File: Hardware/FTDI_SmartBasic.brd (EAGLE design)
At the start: 35.6 x 20.3 mm, 28 parts, among them U1 FT232RLSSOP, U2 MIC5219 3.3V, U3 TS3USB221A

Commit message: Incorporate changes from review
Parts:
- LOGO2: value SFE_LOGO_NAME_FLAME.1_INCH -> SFE_LOGO_FLAME.2_INCH; device SparkFun-Aesthetics:SFE_LOGO_NAME_FLAME_.1 -> SparkFun-Aesthetics:SFE_LOGO_FLAME_.2
- moved LOGO2 5.22 mm to (7.24, 6.60)
- moved JP3 1.27 mm to (14.0, 1.27)
- moved JP2 0.25 mm to (30.5, 1.27)
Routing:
- net V_OUT: track 82.6 -> 81.3 mm
- net N$17: track 15.6 -> 16.9 mm
- net N$16: track 18.5 -> 19.7 mm
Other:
- board text added: "JP1 CLIENT"
- board text added: "JP3 AUX HOST"
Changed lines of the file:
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@@
 <text x="9.652" y="16.383" size="0.8128" layer="21" font="vector" ratio="15" rot="R90" align="bottom-center">5V</text>
 <text x="1.905" y="2.286" size="1.016" layer="16" font="vector" ratio="15" rot="MR270" align="bottom-center">v01</text>
-<text x="8.89" y="2.54" size="0.8128" layer="22" font="vector" ratio="15" rot="MR0" align="bottom-center">DTR</text>
-<text x="11.43" y="2.54" size="0.8128" layer="22" font="vector" ratio="15" rot="MR0" align="bottom-center">TXO</text>
-<text x="13.97" y="2.54" size="0.8128" layer="22" font="vector" ratio="15" rot="MR0" align="bottom-center">RXI</text>
-<text x="16.51" y="2.54" size="0.8128" layer="22" font="vector" ratio="15" rot="MR0" align="bottom-center">VCC</text>
-<text x="19.05" y="2.54" size="0.8128" layer="22" font="vector" ratio="15" rot="MR0" align="bottom-center">CTS</text>
-<text x="21.59" y="2.54" size="0.8128" layer="22" font="vector" ratio="15" rot="MR0" align="bottom-center">GND</text>
+<text x="7.62" y="2.54" size="0.8128" layer="22" font="vector" ratio="15" rot="MR0" align="bottom-center">DTR</text>
+<text x="10.16" y="2.54" size="0.8128" layer="22" font="vector" ratio="15" rot="MR0" align="bottom-center">TXO</text>
+<text x="12.7" y="2.54" size="0.8128" layer="22" font="vector" ratio="15" rot="MR0" align="bottom-center">RXI</text>
+<text x="15.24" y="2.54" size="0.8128" layer="22" font="vector" ratio="15" rot="MR0" align="bottom-center">VCC</text>
+<text x="17.78" y="2.54" size="0.8128" layer="22" font="vector" ratio="15" rot="MR0" align="bottom-center">CTS</text>
+<text x="20.32" y="2.54" size="0.8128" layer="22" font="vector" ratio="15" rot="MR0" align="bottom-center">GND</text>
 <text x="27.94" y="3.048" size="0.8636" layer="22" font="vector" ratio="15" rot="MR0" align="bottom-center">SEL</text>
 <text x="30.48" y="3.048" size="0.8636" layer="22" font="vector" ratio="15" rot="MR0" align="bottom-center">!OE</text>
@@
 <text x="8.255" y="9.652" size="0.8636" layer="22" font="vector" ratio="15" rot="MR0" align="bottom-center">BY</text>
 <text x="-46.99" y="12.7" size="1.778" layer="51" ratio="15" align="bottom-center">M. Hord</text>
-<text x="17.78" y="14.986" size="1.4224" layer="21" font="vector" ratio="15" align="bottom-center">Smart
-   Basic</text>
+<text x="18.161" y="15.875" size="1.4224" layer="21" font="vector" ratio="15" align="bottom-center">Smart
+Basic</text>
+<text x="31.496" y="5.842" size="0.8128" layer="21" font="vector" ratio="15" rot="R90">JP1
+CLIENT</text>
+<text x="31.75" y="18.415" size="0.8128" layer="22" font="vector" ratio="15" rot="SMR270">JP1
+CLIENT</text>
+<text x="11.938" y="6.096" size="0.8128" layer="21" font="vector" ratio="15" rot="R180">JP3
+AUX HOST</text>
+<text x="3.429" y="5.715" size="0.8128" layer="22" font="vector" ratio="15" rot="MR180">JP3
+AUX HOST</text>
 </plain>
 <attributes>
@@
 <attribute name="PROD_ID" value="IC-12115" x="71.755" y="-22.606" size="1.778" layer="27" display="off"/>
 </element>
-<element name="JP3" library="SparkFun-Connectors" package="FTDI_DEVICE_SIDE" value="" x="15.24" y="1.27"/>
+<element name="JP3" library="SparkFun-Connectors" package="FTDI_DEVICE_SIDE" value="" x="13.97" y="1.27"/>
 <element name="JP4" library="SparkFun-Connectors" package="USB-B-MICRO-SMD_V03" value="USB Micro B" x="2.159" y="10.16">
 <attribute name="PROD_ID" value="CONN-11752" x="18.669" y="5.08" size="1.778" layer="27" display="off"/>
@@
 <attribute name="PROD_ID" value="CAP-00810" x="53.721" y="-30.861" size="1.778" layer="27" display="off"/>
 </element>
-<element name="JP2" library="SparkFun-Connectors" package="1X02" value="M02PTH" x="30.48" y="1.524" rot="R180"/>
+<element name="JP2" library="SparkFun-Connectors" package="1X02" value="M02PTH" x="30.48" y="1.27" rot="R180"/>
 <element name="C5" library="SparkFun-Capacitors" package="0603-CAP" value="0.1uF" x="13.97" y="17.78" rot="R90">
 <attribute name="PROD_ID" value="CAP-00810" x="49.53" y="58.42" size="1.778" layer="27" rot="R90" display="off"/>
@@
 <element name="U$1" library="SparkFun-Aesthetics" package="SMART_BASIC_LOGO" value="SMART_BASIC_LOGO" x="32.258" y="3.429" rot="MR0"/>
 <element name="LOGO1" library="SparkFun-Aesthetics" package="SFE_LOGO_NAME_.1" value="SFE_LOGO_NAME.1_INCH" x="11.684" y="5.715" rot="MR0"/>
-<element name="LOGO2" library="SparkFun-Aesthetics" package="SFE_LOGO_NAME_FLAME_.1" value="SFE_LOGO_NAME_FLAME.1_INCH" x="3.302" y="3.175"/>
 <element name="LOGO3" library="SparkFun-Aesthetics" package="OSHW-LOGO-S" value="OSHW-LOGOS" x="2.413" y="1.905"/>
+<element name="LOGO2" library="SparkFun-Aesthetics" package="SFE_LOGO_FLAME_.2" value="SFE_LOGO_FLAME.2_INCH" x="7.239" y="6.604"/>
 </elements>
 <signals>
@@
 <via x="27.94" y="5.969" extent="1-16" drill="0.508"/>
 <wire x1="27.94" y1="5.969" x2="27.94" y2="4.572" width="0.254" layer="1"/>
-<wire x1="27.94" y1="4.572" x2="27.94" y2="1.524" width="0.254" layer="1"/>
+<wire x1="27.94" y1="4.572" x2="27.94" y2="1.27" width="0.254" layer="1"/>
 <wire x1="28.817" y1="4.699" x2="28.067" y2="4.699" width="0.254" layer="1"/>
 <wire x1="28.067" y1="4.699" x2="27.94" y2="4.572" width="0.2032" layer="1"/>
@@
 <wire x1="29.198" y1="7.124" x2="29.972" y2="6.35" width="0.254" layer="1"/>
 <wire x1="29.972" y1="6.35" x2="30.48" y2="5.842" width="0.254" layer="1"/>
-<wire x1="30.48" y1="1.524" x2="30.48" y2="5.842" width="0.254" layer="1"/>
+<wire x1="30.48" y1="1.27" x2="30.48" y2="5.842" width="0.254" layer="1"/>
 <wire x1="30.353" y1="9.652" x2="30.353" y2="11.215" width="0.254" layer="1"/>
 <wire x1="30.353" y1="9.652" x2="30.353" y2="6.731" width="0.2032" layer="16"/>
@@
 <via x="12.954" y="15.621" extent="1-16" drill="0.508"/>
 <wire x1="12.954" y1="15.621" x2="12.954" y2="19.431" width="0.254" layer="16"/>
-<wire x1="16.51" y1="1.27" x2="16.51" y2="2.667" width="0.8128" layer="16"/>
-<wire x1="16.51" y1="2.667" x2="15.875" y2="3.175" width="0.8128" layer="16"/>
-<wire x1="15.875" y1="3.175" x2="3.175" y2="3.175" width="0.8128" layer="16"/>
+<wire x1="15.24" y1="1.27" x2="15.24" y2="2.667" width="0.8128" layer="16"/>
+<wire x1="15.24" y1="2.667" x2="14.605" y2="3.175" width="0.8128" layer="16"/>
+<wire x1="14.605" y1="3.175" x2="3.175" y2="3.175" width="0.8128" layer="16"/>
 <wire x1="3.175" y1="3.175" x2="2.54" y2="3.81" width="0.8128" layer="16"/>
 <wire x1="2.54" y1="3.81" x2="2.54" y2="16.51" width="0.8128" layer="16"/>
@@
 <wire x1="24.003" y1="7.239" x2="24.003" y2="4.191" width="0.254" layer="1"/>
 <wire x1="24.003" y1="4.191" x2="23.622" y2="3.81" width="0.254" layer="1"/>
-<wire x1="23.622" y1="3.81" x2="13.843" y2="3.81" width="0.254" layer="1"/>
-<wire x1="13.843" y1="3.81" x2="12.7" y2="2.667" width="0.254" layer="1"/>
-<wire x1="12.7" y1="2.667" x2="11.43" y2="1.27" width="0.254" layer="1"/>
+<wire x1="23.622" y1="3.81" x2="12.7" y2="3.81" width="0.254" layer="1"/>
+<wire x1="12.7" y1="3.81" x2="10.16" y2="1.27" width="0.254" layer="1"/>
 </signal>
 <signal name="N$17">
@@
 <wire x1="24.638" y1="6.604" x2="24.638" y2="3.683" width="0.254" layer="1"/>
 <wire x1="24.638" y1="3.683" x2="23.876" y2="2.921" width="0.254" layer="1"/>
-<wire x1="23.876" y1="2.921" x2="15.621" y2="2.921" width="0.254" layer="1"/>
-<wire x1="15.621" y1="2.921" x2="13.97" y2="1.27" width="0.254" layer="1"/>
+<wire x1="23.876" y1="2.921" x2="14.351" y2="2.921" width="0.254" layer="1"/>
+<wire x1="14.351" y1="2.921" x2="12.7" y2="1.27" width="0.254" layer="1"/>
 </signal>
 <signal name="N$2">

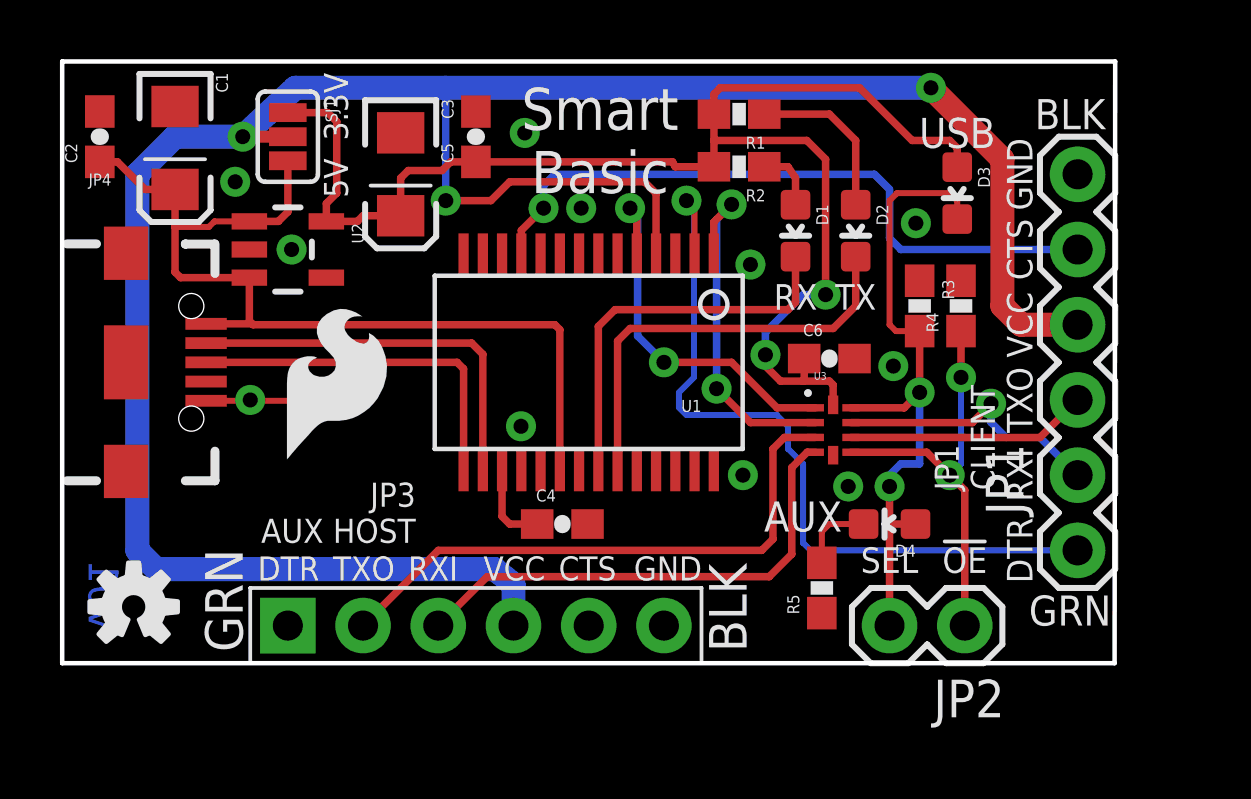
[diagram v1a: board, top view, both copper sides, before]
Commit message: 2nd round protos - add vias to strain relief pads on connector - flip the client connector - remove the USB indicator LED and change other LED label - change silk from JP1 and JP3 to HOST and CLIENT
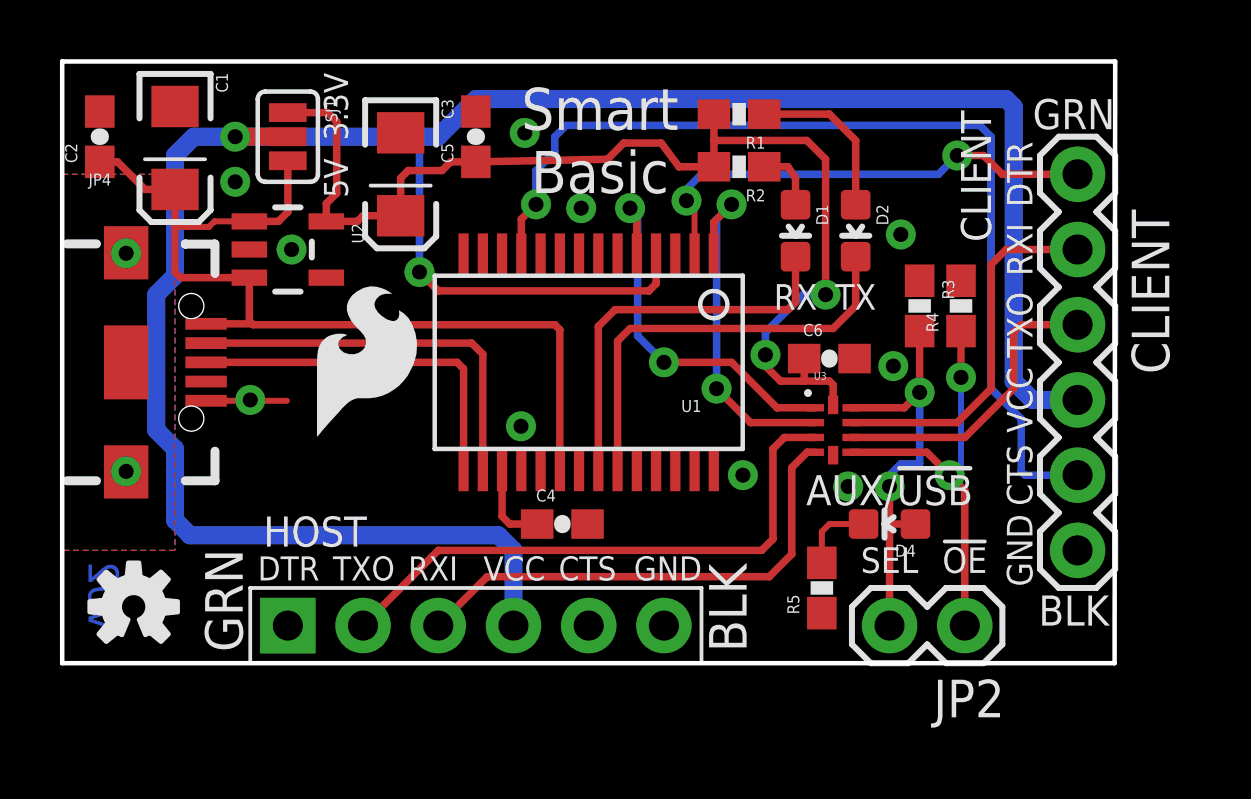
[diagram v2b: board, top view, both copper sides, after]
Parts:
- removed D3: GREEN, SparkFun-LED:LED-0603
- removed JP1: (no value), SparkFun-Connectors:FTDI_BASIC
- added CLIENT: (no value), SparkFun-Connectors:FTDI_BASIC
- moved LOGO2 1.27 mm to (8.26, 7.37)
- renumbered JP3 to HOST
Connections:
- new net SHIELD_POUR: JP4.SHIELD1, JP4.SHIELD2, JP4.SHIELD3
- net 3.3V: no longer D3.A
- net CTS: now also CLIENT.CTS; no longer JP1.CTS
- net DTR: now also CLIENT.DTR; no longer JP1.DTR
- net GND: now also CLIENT.GND; no longer JP1.GND
- net N$13: now also CLIENT.RXI; no longer JP1.RXI
- net N$14: now also CLIENT.TXO; no longer JP1.TXO
- net SELECT: no longer D3.C
- net V_OUT: now also CLIENT.VCC; no longer JP1.VCC
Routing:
- net CTS: track 22.8 -> 33.2 mm
- net DTR: track 26.7 -> 16.6 mm, vias 1 -> 2
- net 3.3V: track 48.6 -> 38.7 mm
- net SELECT: track 22.6 -> 14.2 mm
- net N$13: track 9.29 -> 12.5 mm, vias 1 -> 0
- net V_OUT: track 81.3 -> 84.0 mm, vias 3 -> 2
- net N$14: track 8.18 -> 10.3 mm
- net GND: vias 11 -> 10
- added copper zone on layer 1, net SHIELD_POUR
- added copper zone on layer 16, net SHIELD_POUR
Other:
- board text added: "AUX/!USB"
- board text added: "CLIENT"
- board text added: "HOST"
- board text added: "v02"
- board text removed: "AUX"
- board text removed: "USB"
- board text removed: "v01"

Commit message: Ready for review for reds
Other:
- board text added: "v10"
- board text removed: "v02"
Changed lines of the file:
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@@
 <text x="9.652" y="18.796" size="0.8128" layer="21" font="vector" ratio="15" rot="R90" align="bottom-center">3.3V</text>
 <text x="9.652" y="16.383" size="0.8128" layer="21" font="vector" ratio="15" rot="R90" align="bottom-center">5V</text>
-<text x="1.905" y="2.286" size="1.016" layer="16" font="vector" ratio="15" rot="MR270" align="bottom-center">v02</text>
+<text x="1.905" y="2.286" size="1.016" layer="16" font="vector" ratio="15" rot="MR270" align="bottom-center">v10</text>
 <text x="7.62" y="2.54" size="0.8128" layer="22" font="vector" ratio="15" rot="MR0" align="bottom-center">DTR</text>
 <text x="10.16" y="2.54" size="0.8128" layer="22" font="vector" ratio="15" rot="MR0" align="bottom-center">TXO</text>
